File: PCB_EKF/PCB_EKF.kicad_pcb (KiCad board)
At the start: 2 copper layers, 97.8 x 84.6 mm, 39 parts, among them J1 Load, J2 5V, J4 UART, K1 SANYOU_SRD_Form_C, K3 SANYOU_SRD_Form_C, Q1 Q_NMOS_GDS, Q2 Q_NMOS_GDS, SW1 SW_Push_SPDT, U1 MCP6002-xSN, U2 ACS712-20A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

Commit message: add firmware and change PCB
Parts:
- removed C1, C2, C3: 100nF, Capacitor_SMD:C_0805_2012Metric
- removed U2: ACS712-20A, EKF:ACS712_Module
- added C8: 100nF, Capacitor_SMD:C_0805_2012Metric, F.Cu at (119.1, 99.8)
- added D6: LED, LED_SMD:LED_0805_2012Metric_Pad1.15x1.40mm_HandSolder, F.Cu at (101.6, 106.2)
- added D7: LED, LED_SMD:LED_0805_2012Metric_Pad1.15x1.40mm_HandSolder, F.Cu at (104.4, 106.2)
- added D8: LED, LED_SMD:LED_0805_2012Metric_Pad1.15x1.40mm_HandSolder, F.Cu at (107.2, 106.2)
- added JP1: Jumper_2_Open, Jumper:SolderJumper-2_P1.3mm_Open_RoundedPad1.0x1.5mm, F.Cu at (101.9, 55.9)
- added JP2: Force Control, Connector_PinHeader_2.54mm:PinHeader_1x03_P2.54mm_Vertical, F.Cu at (109.5, 55.9)
- R1: value 47k -> Shunt; footprint Resistor_SMD:R_0805_2012Metric -> Resistor_SMD:R_2512_6332Metric_Pad1.40x3.35mm_HandSolder
- R2: value 100k -> R
- R3: value 1k -> R
- R4: value 10k -> R
- U1: value MCP6002-xSN -> INA226_module; footprint Package_SO:SOIC-8_3.9x4.9mm_P1.27mm -> EKF:INA226_module
- moved U4 93.7 mm to (137.8, 47.9), turned to 180 degrees
- moved J1 89.9 mm to (75.7, 34.7), turned to 180 degrees
- moved R3 71.9 mm to (104.4, 102.5), turned to -90 degrees
- moved J2 71.3 mm to (88.4, 34.8), turned to 180 degrees
- moved R4 68.5 mm to (107.2, 102.5)
- moved R2 65.7 mm to (101.6, 102.5)
- moved C5 59.2 mm to (94.5, 35.5), turned to 90 degrees
- moved C4 53.7 mm to (94.5, 39.4), turned to -90 degrees
- moved R6 51.5 mm to (75.1, 109.5), turned to 0 degrees
- moved U1 49.6 mm to (77.0, 56.3)
- moved U5 49.1 mm to (100.5, 37.2)
- moved Q1 47.5 mm to (75.0, 106.2), turned to 180 degrees
- moved R11 44.9 mm to (106.7, 35.0), turned to -90 degrees
- moved R7 44.6 mm to (74.1, 101.9), turned to 0 degrees
- moved R5 42.2 mm to (78.4, 106.2), turned to -90 degrees
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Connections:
- K1 pad 1: PA+ -> Shunt-
- K3 pad 1: PA+ -> Shunt-
- R1 pad 1: Vbatt+ -> Shunt+
- R1 pad 2: Net-(U1A-+) -> Shunt-
- R2 pad 1: Net-(U1A-+) -> indikator_1
- R2 pad 2: GND -> Net-(D6-A)
- R3 pad 1: Current_Sensor -> indikator_2
- R3 pad 2: Net-(U1B-+) -> Net-(D7-A)
- R4 pad 1: Net-(U1B-+) -> indikator_3
- R4 pad 2: GND -> Net-(D8-A)
- SW1 pad 1: Vbatt+ -> Vbatt
- U1 pad 1: ADC_Vbatt -> Net-(BT1-+)
- U1 pad 2: ADC_Vbatt -> Shunt-
- U1 pad 3: Net-(U1A-+) -> Vbatt
- U1 pad 4: GND -> Alert
- U1 pad 5: Net-(U1B-+) -> SCL
- U1 pad 6: ADC_Current -> SDA
- U1 pad 7: ADC_Current -> GND
- U3 pad 1: CTRL_Load -> unconnected-(U3-PB12-Pad1)
- U3 pad 11: unconnected-(U3-PB3-Pad11) -> indikator_1
- U3 pad 12: unconnected-(U3-PB4-Pad12) -> indikator_2
- U3 pad 13: unconnected-(U3-PB5-Pad13) -> indikator_3
- U3 pad 14: unconnected-(U3-PB6-Pad14) -> SCL
- U3 pad 15: unconnected-(U3-PB7-Pad15) -> SDA
- U3 pad 2: CTRL_Charge -> CTRL_Load
- U3 pad 23: ADC_Vbatt -> unconnected-(U3-PA0-Pad23)
- U3 pad 24: ADC_Current -> unconnected-(U3-PA1-Pad24)
- U3 pad 3: unconnected-(U3-PB14-Pad3) -> CTRL_Charge
- U3 pad 31: unconnected-(U3-PB0-Pad31) -> Alert
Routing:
- net 5V: track 0.00 -> 203.5 mm
- net 3V3: track 0.00 -> 149.9 mm, vias 0 -> 1
- net Shunt-: track 0.00 -> 86.2 mm
- net CTRL_Load: track 0.00 -> 84.9 mm, vias 0 -> 2
- net Net-(BT1-+): track 0.00 -> 80.7 mm
- net Alert: track 0.00 -> 71.4 mm
- net Load: track 0.00 -> 71.0 mm
- net SDA: track 0.00 -> 61.6 mm
- net SCL: track 0.00 -> 61.6 mm
- net CTRL_Charge: track 0.00 -> 61.1 mm
- net Charge: track 0.00 -> 43.7 mm, vias 0 -> 1
- net indikator_1: track 0.00 -> 22.9 mm
- net indikator_2: track 0.00 -> 19.3 mm
- net Vbatt: track 0.00 -> 19.2 mm
- net Net-(D3-K): track 0.00 -> 17.7 mm
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- added copper zone on B.Cu, net GND
- added copper zone on F.Cu, net GND

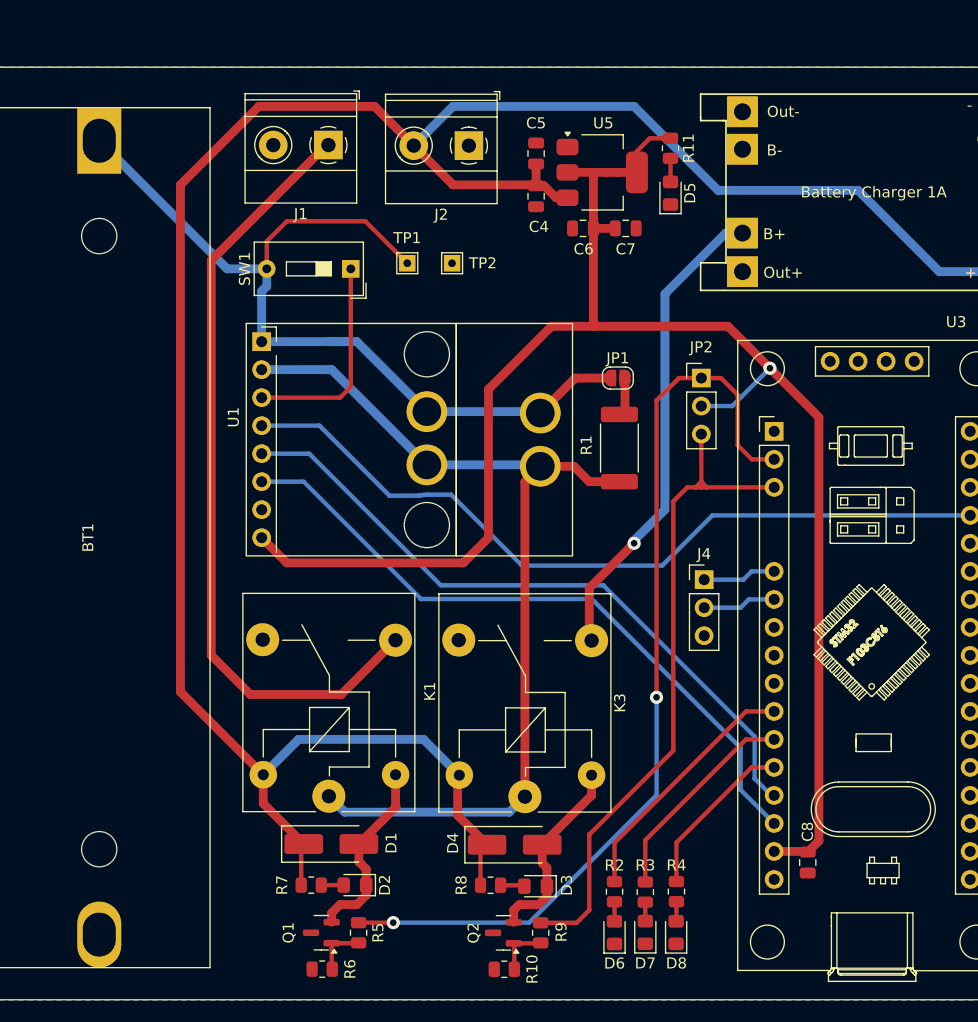
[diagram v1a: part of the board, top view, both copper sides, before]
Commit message: minor change silkscreen
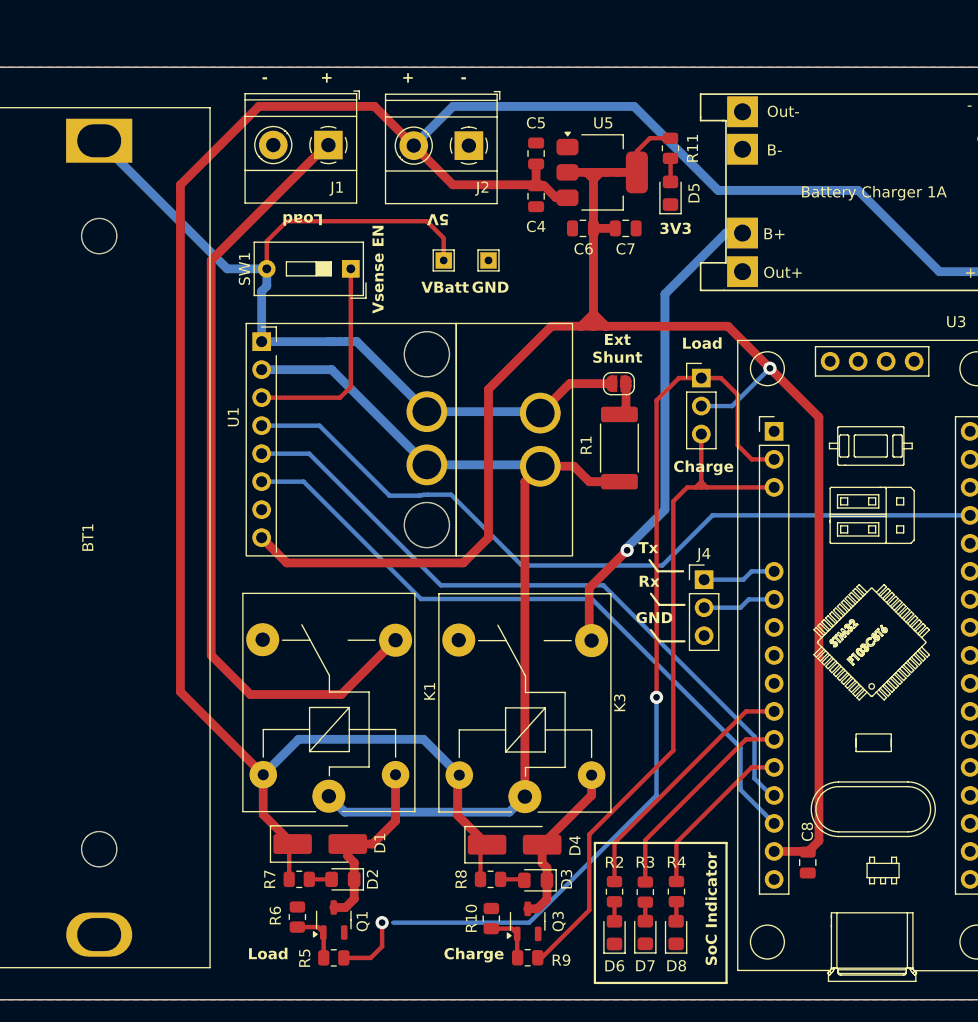
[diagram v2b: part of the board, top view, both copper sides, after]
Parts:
- removed Q2: Q_NMOS_GDS, Package_TO_SOT_SMD:SOT-23
- added Q3: Q_NMOS_GSD, Package_TO_SOT_SMD:SOT-23-3, F.Cu at (93.7, 105.2)
- Q1: value Q_NMOS_GDS -> Q_NMOS_GSD; footprint Package_TO_SOT_SMD:SOT-23 -> Package_TO_SOT_SMD:SOT-23-3
- moved R6 5.24 mm to (72.8, 104.8), turned to -90 degrees
- moved R10 4.75 mm to (90.4, 104.9), turned to -90 degrees
- moved TP2 3.31 mm to (90.2, 45.2)
- moved TP1 3.31 mm to (86.1, 45.2)
- moved R5 3.20 mm to (76.1, 108.5), turned to 180 degrees
- moved R9 2.55 mm to (93.7, 108.5), turned to 180 degrees
- moved Q1 1.61 mm to (76.1, 105.0), turned to 90 degrees
- moved D2 1.21 mm to (77.0, 101.3)
- moved R7 1.21 mm to (73.0, 101.3)
- moved D1 1.01 mm to (74.9, 98.1)
- moved D3 0.54 mm to (94.4, 101.4)
- moved R8 0.54 mm to (90.4, 101.3)
- moved JP1 0.52 mm to (102.0, 56.4)
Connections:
- Q1 pad 2: Net-(D1-A) -> GND
- Q1 pad 3: GND -> Net-(D1-A)
- U3 pad 38: unconnected-(U3-GND-Pad38) -> GND
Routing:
- net 3V3: track 149.9 -> 154.9 mm
- net Net-(BT1-+): track 80.7 -> 85.0 mm
- net CTRL_Load: track 84.9 -> 87.8 mm
- net Net-(D3-K): track 17.7 -> 15.9 mm
- net CTRL_Charge: track 61.1 -> 62.7 mm
- net 5V: track 203.5 -> 202.6 mm
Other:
- board text added: "+"
- board text added: "-"
- board text added: "3V3"
- board text added: "5V"
- board text added: "Charge"
- board text added: "Ext Shunt"
- board text added: "GND"
- board text added: "Load"
- board text added: "Rx"
- board text added: "SoC Indicator"
- board text added: "Tx"
- board text added: "VBatt"
- board text added: "Vsense EN"

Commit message: add a lot
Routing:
- net CTRL_Load: track 87.8 -> 88.8 mm
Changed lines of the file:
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@@
 			(outputformat 1)
 			(mirror no)
-			(drillshape 1)
+			(drillshape 0)
 			(scaleselection 1)
-			(outputdirectory "")
+			(outputdirectory "Gerber/")
 		)
 	)
@@
 		(fp_arc
 			(start 5.210659 19.015233)
-			(mid 5.273125 18.98719)
+			(mid 5.273123 18.987169)
 			(end 5.341329 18.993348)
 			(stroke
@@
 		(fp_arc
 			(start 6.981719 17.244173)
-			(mid 7.051919 17.214426)
+			(mid 7.051919 17.214488)
 			(end 7.121632 17.245341)
 			(stroke
@@
 		(fp_arc
 			(start 8.464456 19.37686)
-			(mid 8.346161 19.099702)
+			(mid 8.346155 19.099702)
 			(end 8.463393 18.822096)
 			(stroke
@@
 		(fp_arc
 			(start 8.924989 18.360501)
-			(mid 9.075715 18.294215)
+			(mid 9.075715 18.294151)
 			(end 9.227336 18.358376)
 			(stroke
@@
 		(fp_arc
 			(start 9.017838 18.458024)
-			(mid 9.077292 18.432027)
+			(mid 9.077292 18.432091)
 			(end 9.136717 18.458131)
 			(stroke
@@
 		(fp_arc
 			(start 11.989999 48.971818)
-			(mid 11.906797 49.125261)
+			(mid 11.906813 49.12524)
 			(end 11.739999 49.176605)
 			(stroke
@@
 		(fp_arc
 			(start 11.99 49.115212)
-			(mid 11.906844 49.268701)
+			(mid 11.906816 49.268638)
 			(end 11.739999 49.32)
 			(stroke
@@
 		(fp_arc
 			(start 12.464857 49.004759)
-			(mid 12.372292 48.850875)
+			(mid 12.372274 48.85088)
 			(end 12.340011 48.674215)
 			(stroke
@@
 		(fp_arc
 			(start 12.648833 48.840847)
-			(mid 12.603027 48.765284)
+			(mid 12.603045 48.765279)
 			(end 12.586427 48.6785)
 			(stroke
@@
 		)
 		(property "Value" "1k"
-			(at 0 1.65 360)
+			(at 0 1.65 0)
 			(layer "F.Fab")
 			(effects
@@
 		)
 		(fp_text user "${REFERENCE}"
-			(at 0 0 360)
+			(at 0 0 0)
 			(layer "F.Fab")
 			(effects
@@
 		(tags "resistor")
 		(property "Reference" "R9"
-			(at -3.048 -0.254 360)
+			(at -3.048 -0.254 0)
 			(layer "F.SilkS")
 			(effects
@@
 		)
 		(property "Value" "1k"
-			(at 0 1.65 360)
+			(at 0 1.65 0)
 			(layer "F.Fab")
 			(effects
@@
 		)
 		(fp_text user "${REFERENCE}"
-			(at 0 0 360)
+			(at 0 0 0)
 			(layer "F.Fab")
 			(effects
@@
 	(segment
 		(start 93.8605 105.2755)
-		(end 81.534 105.2755)
+		(end 80.5225 105.2755)
 		(width 0.4)
 		(layer "B.Cu")
